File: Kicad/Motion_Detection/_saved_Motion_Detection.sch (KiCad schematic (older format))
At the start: 38 parts, among them J1 12V input, J2 SE-10, J3 SEN0192_MW, J4 EKMB, J5 3V3 Output, J6 ZRE200GE, J7 5V Ext, J8 3V3 EN, P1 XBee, U1 LM7805_TO220, U2 LM324

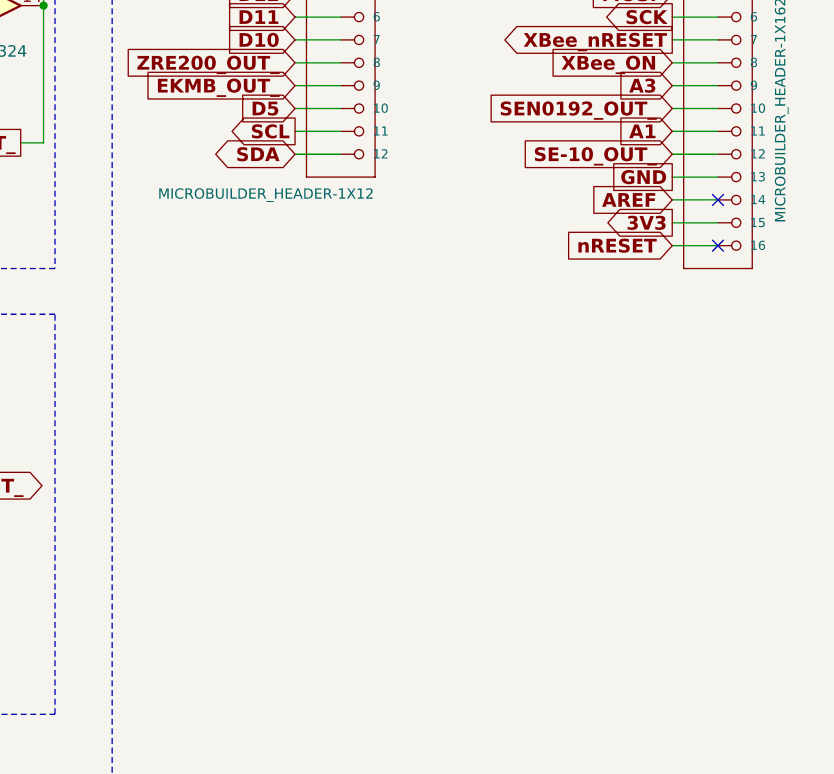
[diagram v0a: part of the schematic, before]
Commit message: Status led pin added to schematic and PCB.
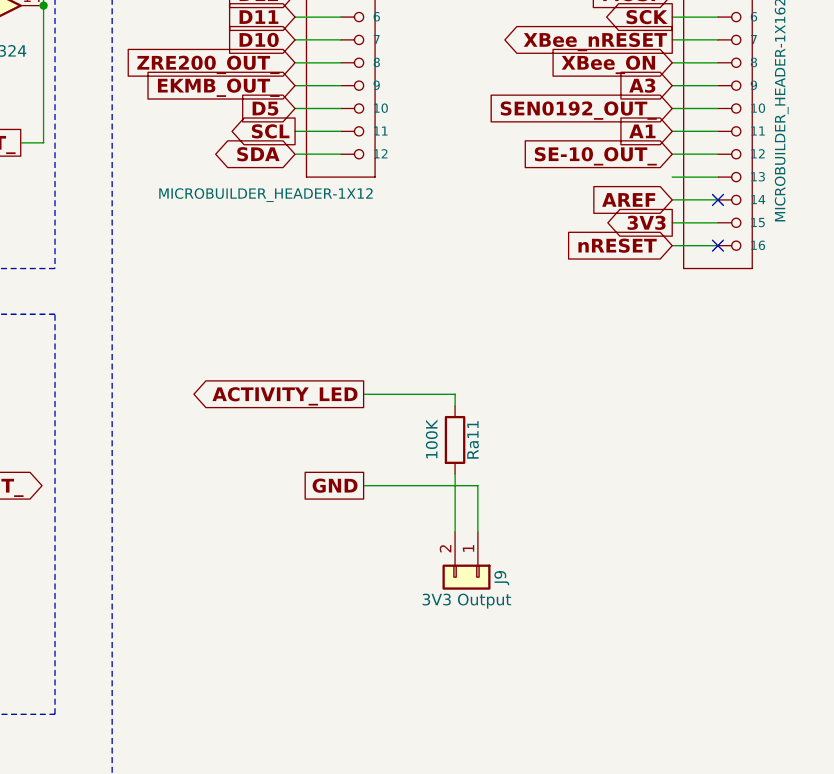
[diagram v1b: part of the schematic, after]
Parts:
- added J9: 3V3 Output, Connectors_Molex:Molex_KK-6410-02_02x2.54mm_Straight, symbol Conn_01x02
- added Ra11: 100K, Resistors_THT:R_Axial_DIN0207_L6.3mm_D2.5mm_P7.62mm_Horizontal, symbol R
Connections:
- net ACTIVITY_LED: now also Ra11.1
- net GND: now also J9.1 (Pin_1); no longer JP2.13
- new net: J9.2 (Pin_2), Ra11.2
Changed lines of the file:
@@
 Text GLabel 10000 2700 0    60   Input ~ 12
 SE-10_OUT_
-Text GLabel 10000 2800 0    60   UnSpc ~ 12
+Text GLabel 8650 4150 0    60   UnSpc ~ 12
 GND
 Text GLabel 10000 3000 0    60   Output ~ 12
@@
 	1500 1000 1500 950
 Connection ~ 1500 1000
+$Comp
+L Conn_01x02 J9
+U 1 1 5A11B7B1
+P 9150 4550
+F 0 "J9" H 9150 4650 50  0000 C CNN
+F 1 "3V3 Output" V 9250 4500 50  0000 C CNN
+F 2 "Connectors_Molex:Molex_KK-6410-02_02x2.54mm_Straight" H 9150 4550 50  0001 C CNN
+F 3 "" H 9150 4550 50  0001 C CNN
+	1    9150 4550
+	0    1    1    0
+$EndComp
+Text GLabel 8650 3750 0    60   Output ~ 12
+ACTIVITY_LED
+$Comp
+L R Ra11
+U 1 1 5A11C1D6
+P 9050 3950
+F 0 "Ra11" V 9130 3950 50  0000 C CNN
+F 1 "100K" V 8950 3950 50  0000 C CNN
+F 2 "Resistors_THT:R_Axial_DIN0207_L6.3mm_D2.5mm_P7.62mm_Horizontal" V 8980 3950 50  0001 C CNN
+F 3 "" H 9050 3950 50  0001 C CNN
+	1    9050 3950
+	1    0    0    -1
+$EndComp
+Wire Wire Line
+	8650 3750 9050 3750
+Wire Wire Line
+	9050 3750 9050 3800
+Wire Wire Line
+	8650 4150 9150 4150
+Wire Wire Line
+	9150 4150 9150 4350
+Wire Wire Line
+	9050 4100 9050 4350
 $EndSCHEMATC
